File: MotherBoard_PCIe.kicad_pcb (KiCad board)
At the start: 2 copper layers, 90 x 196 mm, 40 parts, among them J1 Conn_01x02, J10 Bus_mechaken_PCIexpress_x16_1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, J11 Conn_01x03, J12 Conn_01x03, J2 Conn_01x02, J3 Conn_01x07, J4 Conn_01x07, J5 Bus_mechaken_PCIexpress_x16_1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, J6 Bus_mechaken_PCIexpress_x16_1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, J7 Bus_mechaken_PCIexpress_x16_1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, J8 Bus_mechaken_PCIexpress_x16_1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, J9 Bus_mechaken_PCIexpress_x16_1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, U1 L7812

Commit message: clean
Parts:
- moved J11 2.00 mm to (142.5, 153.5)
- moved J12 1.75 mm to (142.8, 78.5)
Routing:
- net +12V: track 190.4 -> 194.2 mm
- net Net-(J12-Pad3): vias 0 -> 1
- net Net-(J11-Pad3): vias 0 -> 1
- net GNDPWR: vias 250 -> 248
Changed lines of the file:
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@@
   )
   (setup
-    (last_trace_width 0.4)
+    (last_trace_width 0.25)
     (user_trace_width 0.2)
     (user_trace_width 0.4)
@@
   )
   (module Connector:FanPinHeader_1x03_P2.54mm_Vertical (layer F.Cu)
-    (at 144.5 78.5 90)
+    (at 142.75 78.5 90)
     (descr "3-pin CPU fan Through hole pin header, see http://www.formfactors.org/developer%5Cspecs%5Crev1_2_public.pdf")
     (tags "pin header 3-pin CPU fan")
@@
   )
   (module Connector:FanPinHeader_1x03_P2.54mm_Vertical (layer F.Cu)
-    (at 144.5 153.5 90)
+    (at 142.5 153.5 90)
     (descr "3-pin CPU fan Through hole pin header, see http://www.formfactors.org/developer%5Cspecs%5Crev1_2_public.pdf")
     (tags "pin header 3-pin CPU fan")
@@
   (via (at 142 83.5) (size 0.6) (drill 0.3) (layers F.Cu B.Cu) (net 2))
   (via (at 142 78.5) (size 0.6) (drill 0.3) (layers F.Cu B.Cu) (net 2))
-  (via (at 142 73.5) (size 0.6) (drill 0.3) (layers F.Cu B.Cu) (net 2))
+  (via (at 142 73.5) (size 0.6) (drill 0.3) (layers F.Cu B.Cu) (net 13))
   (via (at 142 68.5) (size 0.6) (drill 0.3) (layers F.Cu B.Cu) (net 2))
   (via (at 117 93.5) (size 0.6) (drill 0.3) (layers F.Cu B.Cu) (net 2))
@@
   (via (at 142 158.5) (size 0.6) (drill 0.3) (layers F.Cu B.Cu) (net 2))
   (via (at 142 153.5) (size 0.6) (drill 0.3) (layers F.Cu B.Cu) (net 2))
-  (via (at 142 148.5) (size 0.6) (drill 0.3) (layers F.Cu B.Cu) (net 2))
+  (via (at 142 148.5) (size 0.6) (drill 0.3) (layers F.Cu B.Cu) (net 11))
   (via (at 142 143.5) (size 0.6) (drill 0.3) (layers F.Cu B.Cu) (net 2))
   (via (at 117 168.5) (size 0.6) (drill 0.3) (layers F.Cu B.Cu) (net 2))
@@
   (segment (start 146 201) (end 146.25 200.75) (width 0.4) (layer F.Cu) (net 12))
   (segment (start 146.25 200.75) (end 146.25 149.75) (width 0.4) (layer F.Cu) (net 12))
-  (segment (start 145.5 76.96) (end 144.5 75.96) (width 0.4) (layer F.Cu) (net 12))
-  (segment (start 146.25 77.71) (end 145.5 76.96) (width 0.4) (layer F.Cu) (net 12))
-  (segment (start 146.25 152.25) (end 146.25 77.71) (width 0.4) (layer F.Cu) (net 12))
-  (segment (start 144.5 150.96) (end 144.96 150.96) (width 0.4) (layer F.Cu) (net 12))
   (segment (start 144.96 150.96) (end 146.25 152.25) (width 0.4) (layer F.Cu) (net 12))
+  (segment (start 142.5 150.96) (end 144.96 150.96) (width 0.4) (layer F.Cu) (net 12))
+  (segment (start 146.25 152.25) (end 146.25 77.71) (width 0.4) (layer F.Cu) (net 12))
+  (segment (start 146.25 77.71) (end 144.5 75.96) (width 0.4) (layer F.Cu) (net 12))
+  (segment (start 144.5 75.96) (end 142.75 75.96) (width 0.4) (layer F.Cu) (net 12))
   (zone (net 2) (net_name GNDPWR) (layer F.Cu) (hatch edge 0.508)
     (priority 5)

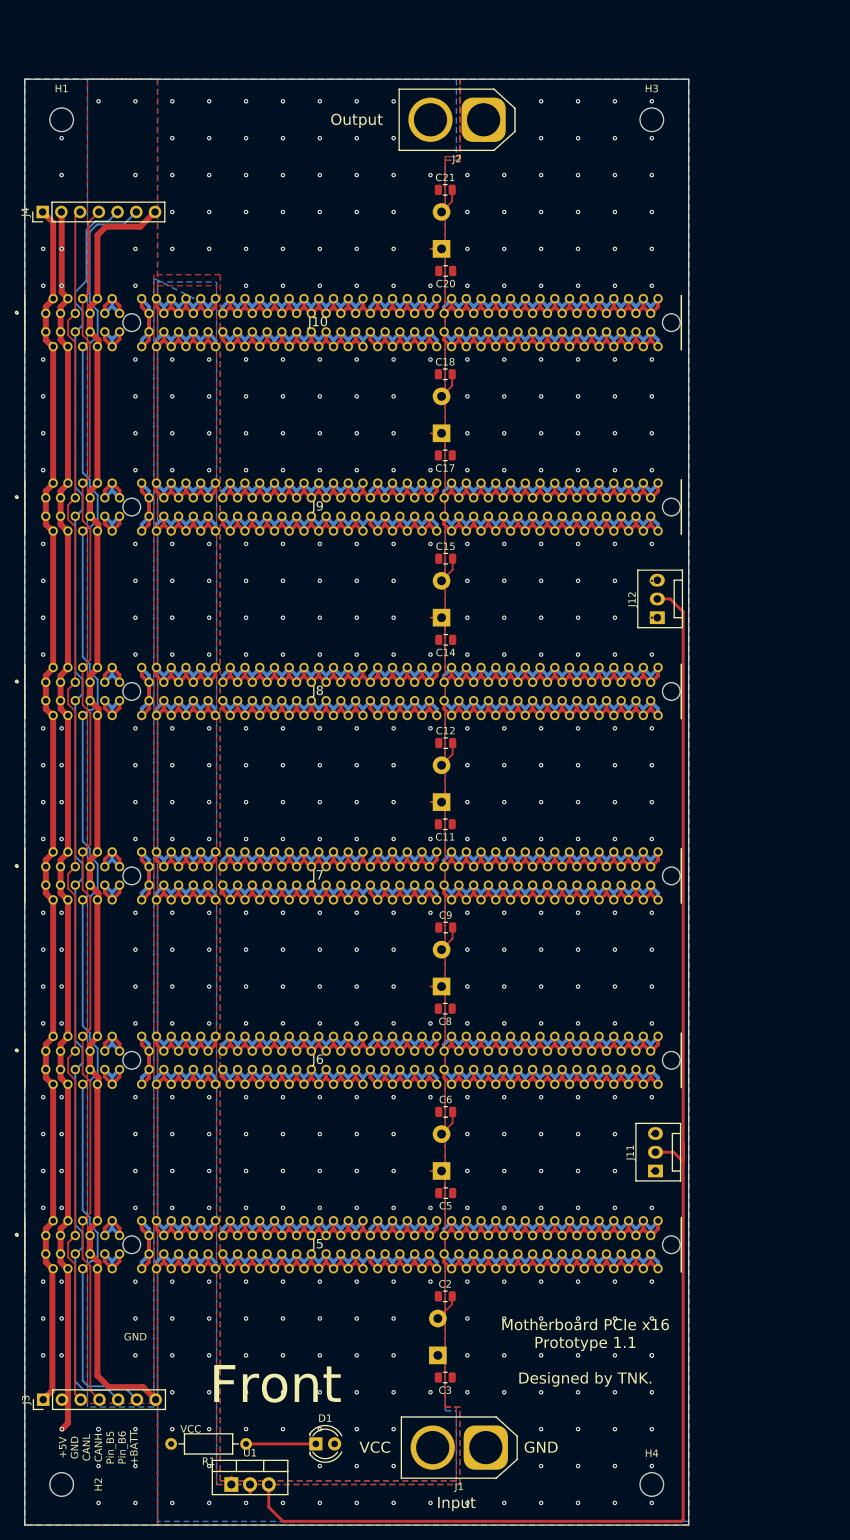
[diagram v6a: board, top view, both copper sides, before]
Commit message: add
通電確認用LEDとファンコネクタを1つ追加
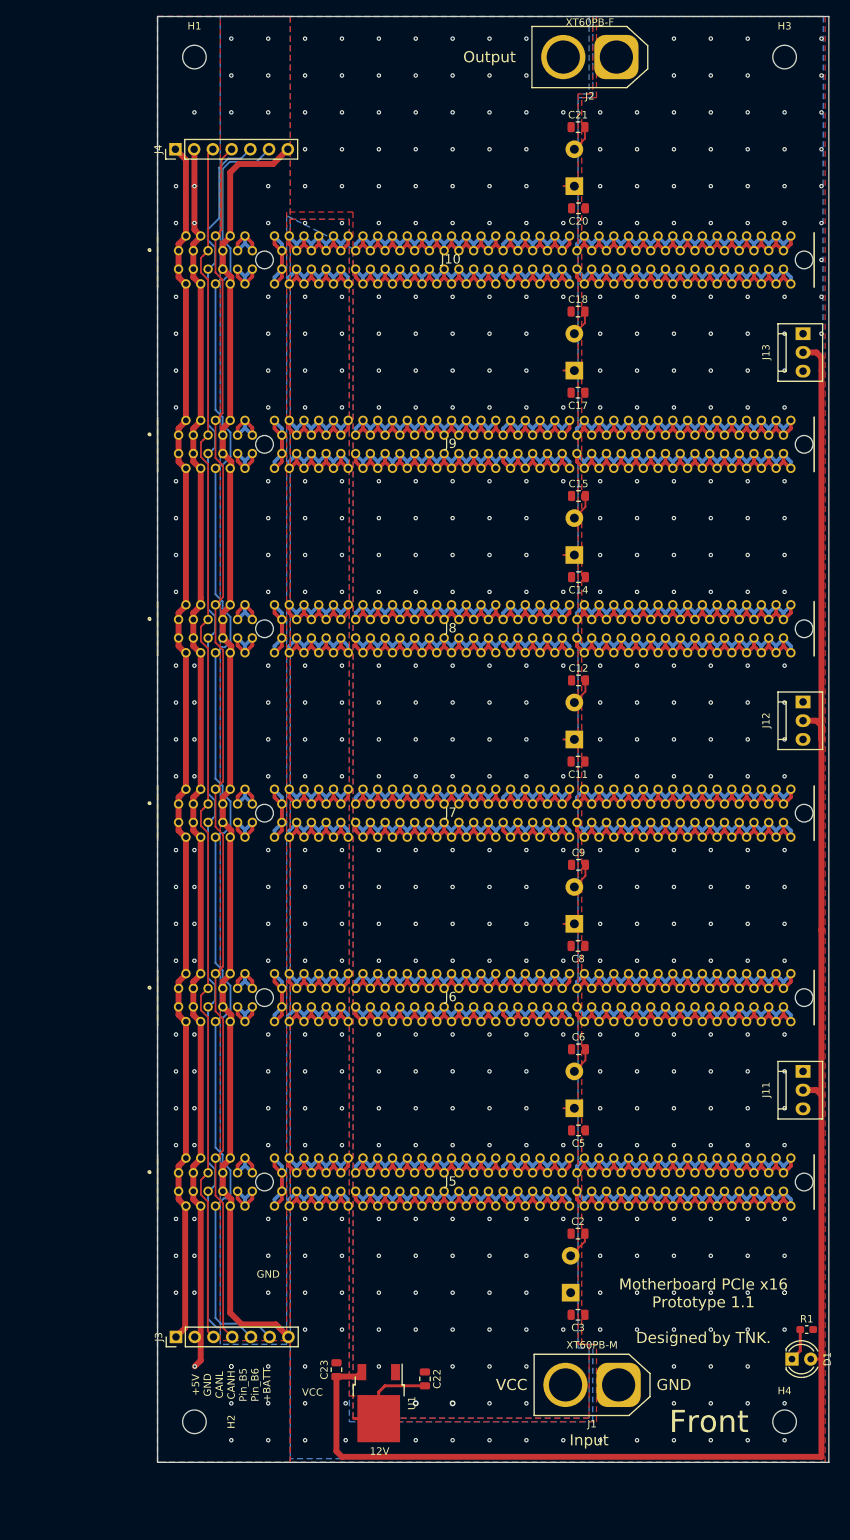
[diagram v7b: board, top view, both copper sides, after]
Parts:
- added C22: 0.47u, Capacitor_SMD:C_0805_2012Metric, F.Cu at (111.2, 181.7)
- added C23: 0.1u, Capacitor_SMD:C_0805_2012Metric, F.Cu at (99.2, 180.4)
- added J13: Conn_01x03, Connector:FanPinHeader_1x03_P2.54mm_Vertical, F.Cu at (162.5, 40.0)
- J1: value Conn_01x02 -> XT60PB-M
- J2: value Conn_01x02 -> XT60PB-F
- R1: footprint Resistor_THT:R_Axial_DIN0207_L6.3mm_D2.5mm_P10.16mm_Horizontal -> Resistor_SMD:R_0603_1608Metric_Pad1.05x0.95mm_HandSolder
- U1: value L7812 -> 12V; footprint Package_TO_SOT_THT:TO-220-3_Vertical -> Package_TO_SOT_SMD:TO-252-2
- moved R1 77.6 mm to (163.0, 175.0), turned to 0 degrees
- moved D1 65.6 mm to (161.0, 179.0)
- moved J11 24.1 mm to (162.5, 140.0), turned to 270 degrees
- moved U1 22.8 mm to (105.0, 185.0), turned to 270 degrees
- moved J12 22.8 mm to (162.5, 89.9), turned to 270 degrees
- moved C1 19.9 mm to (131.0, 170.0)
- moved C10 19.9 mm to (131.5, 95.0)
- moved C11 19.9 mm to (132.0, 98.0)
- moved C12 19.9 mm to (132.1, 87.0)
- moved C13 19.9 mm to (131.5, 70.0)
- moved C14 19.9 mm to (132.1, 73.0)
- moved C15 19.9 mm to (132.1, 62.0)
- moved C16 19.9 mm to (131.5, 45.0)
- moved C17 19.9 mm to (132.0, 48.0)
- moved C18 19.9 mm to (132.0, 37.0)
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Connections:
- D1 pad 2: VCC -> +12V
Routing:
- net +12V: track 194.2 -> 240.9 mm
- net GNDPWR: track 1750.5 -> 1762.9 mm, vias 248 -> 257
- net Net-(D1-Pad1): track 9.46 -> 4.47 mm
- net VCC: track 1530.7 -> 1529.7 mm, vias 210 -> 213
- net GND: vias 52 -> 51
- net Net-(J12-Pad3): vias 1 -> 0
- net Net-(J11-Pad3): vias 1 -> 0
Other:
- board size 90 x 196 mm -> 91 x 196 mm
- board text added: "Attention! The maximum value of the total fan current is 800 mA."
- board text added: "C1, C4, C7, C10, C13, C16, C19 -> 1uF C2, C5, C8, C11, C14, C17, C20 -> 1000uF C3, C6, C9, C12, C15, C18, C21 -> 10uF C22 -> 0.47uF, C23 -> 0.1uF"
- board text removed: "C1, C4, C7, C10, C13, C16, C19 -> 1000uF C2, C5, C8, C11, C14, C17, C20 -> 10uF C3, C6, C9, C12, C15, C18, C21 -> 1uF"

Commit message: clean
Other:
- board text added: "C1, C4, C7, C10, C13, C16, C19 -> 1uF C2, C5, C8, C11, C14, C17, C20 -> 1000uF C3, C6, C9, C12, C15, C18, C21 -> 10uF C22 -> 0.33uF, C23 -> 0.1uF"
- board text removed: "C1, C4, C7, C10, C13, C16, C19 -> 1uF C2, C5, C8, C11, C14, C17, C20 -> 1000uF C3, C6, C9, C12, C15, C18, C21 -> 10uF C22 -> 0.47uF, C23 -> 0.1uF"
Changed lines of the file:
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@@
   )
   (setup
-    (last_trace_width 0.8)
+    (last_trace_width 0.25)
     (user_trace_width 0.2)
     (user_trace_width 0.4)
@@
     (effects (font (size 3 3) (thickness 0.45)) (justify mirror))
   )
-  (gr_text "C1, C4, C7, C10, C13, C16, C19 -> 1uF\nC2, C5, C8, C11, C14, C17, C20 -> 1000uF\nC3, C6, C9, C12, C15, C18, C21 -> 10uF\nC22 -> 0.47uF,  C23 -> 0.1uF" (at 165 175) (layer B.SilkS)
+  (gr_text "C1, C4, C7, C10, C13, C16, C19 -> 1uF\nC2, C5, C8, C11, C14, C17, C20 -> 1000uF\nC3, C6, C9, C12, C15, C18, C21 -> 10uF\nC22 -> 0.33uF,  C23 -> 0.1uF" (at 165 175) (layer B.SilkS)
     (effects (font (size 0.8 0.8) (thickness 0.12)) (justify left mirror))
   )
